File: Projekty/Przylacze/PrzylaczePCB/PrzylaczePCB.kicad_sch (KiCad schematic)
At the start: 9 parts, among them J1 Conn_01x06, J2 USB_B, U1 ATSAM4S2AA-AU

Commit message: Przyłącze - schemat elektryczny v1.0
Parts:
- removed C2: 2.2μ, symbol Device:C
- added C2: 4.7μ, Capacitor_THT:CP_Radial_Tantal_D5.0mm_P2.50mm, symbol Device:C_Polarized_US
- added C3: 2.2μ, Capacitor_THT:CP_Radial_Tantal_D5.0mm_P2.50mm, symbol Device:C_Polarized_US
- added D1, D2: LED, LED_SMD:LED_Kingbright_AAA3528ESGCT, symbol Device:LED
- added J1: Conn_02x04_Odd_Even, Connector_PinHeader_2.54mm:PinHeader_2x04_P2.54mm_Vertical, symbol Connector_Generic:Conn_02x04_Odd_Even
- added J2: Conn_02x20_Odd_Even, Connector_PinHeader_2.54mm:PinHeader_2x20_P2.54mm_Vertical, symbol Connector_Generic:Conn_02x20_Odd_Even
- added J5: Screw_Terminal_01x06, symbol Connector:Screw_Terminal_01x06
- added Q1, Q3, Q7, Q8: BC557, Package_TO_SOT_THT:TO-92_Inline, symbol Transistor_BJT:BC557
- added Q2, Q4: BC547, Package_TO_SOT_THT:TO-92_Inline, symbol Transistor_BJT:BC547
- added Q5, Q6: 2N3904, Package_TO_SOT_THT:TO-92_Inline, symbol Transistor_BJT:2N3904
- added R1, R10, R2, R3, R4, R9: 1k, Resistor_THT:R_Axial_DIN0207_L6.3mm_D2.5mm_P7.62mm_Horizontal, symbol Device:R
- added R5, R6: 360, Resistor_THT:R_Axial_DIN0207_L6.3mm_D2.5mm_P7.62mm_Horizontal, symbol Device:R
- added R7, R8: 470k, Resistor_THT:R_Axial_DIN0207_L6.3mm_D2.5mm_P7.62mm_Horizontal, symbol Device:R
- added SW1: SW_Push, Button_Switch_THT:SW_PUSH_6mm, symbol Switch:SW_Push
- added U1, U2: 74AHC1G04, PrzylaczeFootprintLibrary:Nexperia-SOT753-10_2018-0-0, symbol 74xGxx:74AHC1G04
- added U10: LDL1117S33R, Package_TO_SOT_SMD:SOT-223-3_TabPin2, symbol PrzylaczePCBLib:LDL1117S33R
- added U9: DI78M05UAB, Package_TO_SOT_SMD:SOT-89-3, symbol PrzylaczePCBLib:DI78M05UAB
- C1: value 4.7μ -> 100n; footprint (none) -> Capacitor_THT:C_Disc_D3.0mm_W1.6mm_P2.50mm
- J3: renamed from J1; footprint (none) -> Connector_PinHeader_2.54mm:PinHeader_1x06_P2.54mm_Horizontal
- J4: renamed from J2; footprint (none) -> Connector_USB:USB_B_OST_USB-B1HSxx_Horizontal
- R11: renamed from R1; footprint (none) -> Resistor_THT:R_Axial_DIN0207_L6.3mm_D2.5mm_P7.62mm_Horizontal
- R12: renamed from R2; footprint (none) -> Resistor_THT:R_Axial_DIN0207_L6.3mm_D2.5mm_P7.62mm_Horizontal
- R13: renamed from R3; footprint (none) -> Resistor_THT:R_Axial_DIN0207_L6.3mm_D2.5mm_P7.62mm_Horizontal
- R14: renamed from R4; footprint (none) -> Resistor_THT:R_Axial_DIN0207_L6.3mm_D2.5mm_P7.62mm_Horizontal
- U3: renamed from U1; footprint Microchip_Technology-ATSAM4S2AA-AU-* -> Package_QFP:LQFP-48_7x7mm_P0.5mm
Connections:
- net +3V3: now also C1.2, U3.33 (VDDIO), U3.47 (VDDIO), C2.1, J1.2 (Pin_2), J1.4 (Pin_4); no longer C1.1
- net CS0: now also J1.3 (Pin_3), J2.40 (Pin_40)
- net CS3: now also J2.38 (Pin_38)
- net MISO: now also J1.7 (Pin_7), J2.35 (Pin_35)
- net MOSI: now also J1.6 (Pin_6), J2.33 (Pin_33)
- net SPCK: now also J1.5 (Pin_5), J2.37 (Pin_37)
- net USBMON: now also U3.3 (PB0/AD4); no longer U3.31 (PA3)
- net at U3.18 (VDDCORE), U3.48 (VDDPLL), U3.8 (VDDOUT): now also U3.41 (VDDCORE), C3.1
- net RX/TX ENABLE : now reaches U3.28 (PA4/PGMNCMD)
- net at U3.29 (~{RST}): now also SW1.2
- net OPTO_R1: now reaches U3.32 (PA2/PGMEN2)
- net OPTO_R1: now also U3.31 (PA3), J2.16 (Pin_16), J2.18 (Pin_18), Q6.3 (C), R8.1
- net +5V: now reaches U3.34 (GND)
- net +5V: now also C1.1, J3.1 (Pin_1), J4.4 (GND), R14.2, U3.2 (GND), C2.2, C3.2, J1.1 (Pin_1), J5.6 (Pin_6), Q1.3 (E), Q2.3 (E), Q3.3 (E), Q4.3 (E), Q5.1 (E), Q6.1 (E), Q7.3 (E), Q8.3 (E), R7.2, R8.2, SW1.1, U1.3 (GND), U1.5 (VCC), U10.3 (Vin), U2.3 (GND), U2.5 (VCC), U9.1 (Vout), U9.2 (GND)
- net OPTO_SW2: now reaches U3.35 (PA1/PGMEN1)
- net OPTO_SW2: now also J2.14 (Pin_14), R1.2, R9.2, U1.2
- net OPTO_SW1: now reaches U3.36 (PA0/PGMEN0)
- net OPTO_SW1: now also J2.12 (Pin_12), R10.2, R2.2, U2.2
- net RADIO_IRQ: now reaches U3.4 (PB1/AD5)
- net RADIO_IRQ: now also J1.8 (Pin_8)
- net UART1_RX: now reaches U3.5 (PB2/AD6)
- net UART1_TX: now reaches U3.6 (PB3/AD7)
- net CS1 renamed UART0_RX
- net UART0_RX: now also J2.20 (Pin_20)
- net CS2 renamed UART0_TX
- net UART0_TX: now also J2.22 (Pin_22)
- removed net GND: C1.2, J3.1 (Pin_1), J4.4 (GND), R14.2, U3.2 (GND)
- new net: Q8.2 (B), R10.1
- new net: Q8.1 (C), R6.1
- new net: Q3.2 (B), R4.1
- new net: R4.2, U2.4
- new net: Q1.2 (B), R3.1
- new net: R3.2, U1.4
- new net: Q7.1 (C), R5.1
- new net: Q7.2 (B), R9.1
- new net: D2.1 (K), Q3.1 (C), Q4.1 (C)
- new net: Q4.2 (B), R2.1
- new net: D2.2 (A), Q6.2 (B), R6.2
- new net: D1.1 (K), Q1.1 (C), Q2.1 (C)
- new net: Q2.2 (B), R1.1
- new net: D1.2 (A), Q5.2 (B), R5.2
- new net +12V: J5.5 (Pin_5), U10.3 (Vin), U9.3 (Vin)
- new net +3.3V: U10.2 (Vout)
- new net A: J2.2 (Pin_2), J5.1 (Pin_1)
- new net B: J2.4 (Pin_4), J5.2 (Pin_2)
- new net CANH: J2.1 (Pin_1), J5.3 (Pin_3)
- new net CANL: J2.3 (Pin_3), J5.4 (Pin_4)
- new net EN: J2.13 (Pin_13)
- new net ERR: J2.15 (Pin_15)
- new net INT: J2.29 (Pin_29)
- new net OPTO_R2: Q5.3 (C), R7.1
- new net RESET: J2.39 (Pin_39)
- new net RX0BF: J2.23 (Pin_23)
- new net RX1BF: J2.25 (Pin_25)
- new net RXD: J2.7 (Pin_7)
- new net RX_MCU: J2.8 (Pin_8)
- new net RX/TX ENABLE: J2.10 (Pin_10)
- new net SOF: J2.27 (Pin_27)
- new net STB_FT: J2.9 (Pin_9)
- new net TX0RTS: J2.17 (Pin_17)
- new net TX1RTS: J2.19 (Pin_19)
- new net TX2RTS: J2.21 (Pin_21)
- new net TXD: J2.5 (Pin_5)
- new net TX_MCU: J2.6 (Pin_6)
- new net WAKE: J2.11 (Pin_11)
- no-connect marks 0 -> 15
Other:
- added sheet CAN (CAN.kicad_sch)
- added sheet EIA485 (EIA485.kicad_sch)
- note added: "C3 jak najbliżej złącza NRF24L01+ ma wymiary 30 x 16 mm"
- note added: "D1 i D2 dosyć blisko siebie na brzegu płytki"
- note added: "EIA485"
- note added: "JTAG"
- note added: "LISTWA UŻYTKOWNIKA"
- note added: "LISTWA WIĄZKI"
- note added: "Listwa użytkownika na przedniej krawędzi płytki Listwa wiązki, USB, JTAG na tylnej krawędzi płytki Złącze dla RADIO (moduł NRF24L01+) umieścić na tylnej krawędzi płytki tak, aby moduł wystawał poza nią (patrz obrazek po prawo)"
- note added: "Mikrokontroler"
- note added: "OPTO"
- note added: "OPTO EXT_MCU"
- note added: "RADIO"
- note added: "SPI RADIO & CAN"
- note added: "USB"
- note added: "Zasilanie"
- note added: "Złącza"
- moved on the sheet: J3, J4, R11, R12, R13, R14, U3

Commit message: Przyłącze - schemat elektryczny v1.1
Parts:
- J5: footprint (none) -> TerminalBlock:TerminalBlock_bornier-6_P5.08mm
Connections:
- net A: now also J2.1 (Pin_1)
- net B: now also J2.3 (Pin_3)
- net CANH: now also J2.5 (Pin_5), J2.6 (Pin_6); no longer J2.1 (Pin_1)
- net CANL: now also J2.7 (Pin_7), J2.8 (Pin_8); no longer J2.3 (Pin_3)
- net CS0: now also J2.36 (Pin_36); no longer J2.40 (Pin_40)
- net CS3: now also J2.34 (Pin_34); no longer J2.38 (Pin_38)
- net EN: now also J2.17 (Pin_17); no longer J2.13 (Pin_13)
- net ERR: now also J2.19 (Pin_19); no longer J2.15 (Pin_15)
- net INT: now also J2.33 (Pin_33); no longer J2.29 (Pin_29)
- net MISO: now also J2.30 (Pin_30); no longer J2.35 (Pin_35)
- net MOSI: now also J2.28 (Pin_28); no longer J2.33 (Pin_33)
- net OPTO_R1: now also J2.20 (Pin_20), J2.22 (Pin_22); no longer J2.16 (Pin_16), J2.18 (Pin_18)
- net OPTO_SW1: now also J2.16 (Pin_16); no longer J2.12 (Pin_12)
- net OPTO_SW2: now also J2.18 (Pin_18); no longer J2.14 (Pin_14)
- net RESET: now also J2.35 (Pin_35); no longer J2.39 (Pin_39)
- net RX0BF: now also J2.27 (Pin_27); no longer J2.23 (Pin_23)
- net RX1BF: now also J2.29 (Pin_29); no longer J2.25 (Pin_25)
- net RXD: now also J2.11 (Pin_11); no longer J2.7 (Pin_7)
- net RX_MCU: now also J2.12 (Pin_12); no longer J2.8 (Pin_8)
- net RX/TX ENABLE: now also J2.14 (Pin_14); no longer J2.10 (Pin_10)
- net SOF: now also J2.31 (Pin_31); no longer J2.27 (Pin_27)
- net SPCK: now also J2.32 (Pin_32); no longer J2.37 (Pin_37)
- net STB_FT: now also J2.13 (Pin_13); no longer J2.9 (Pin_9)
- net TX0RTS: now also J2.21 (Pin_21); no longer J2.17 (Pin_17)
- net TX1RTS: now also J2.23 (Pin_23); no longer J2.19 (Pin_19)
- net TX2RTS: now also J2.25 (Pin_25); no longer J2.21 (Pin_21)
- net TXD: now also J2.9 (Pin_9); no longer J2.5 (Pin_5)
- net TX_MCU: now also J2.10 (Pin_10); no longer J2.6 (Pin_6)
- net UART0_RX: now also J2.24 (Pin_24); no longer J2.20 (Pin_20)
- net UART0_TX: now also J2.26 (Pin_26); no longer J2.22 (Pin_22)
- net WAKE: now also J2.15 (Pin_15); no longer J2.11 (Pin_11)
- no-connect marks 15 -> 19
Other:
- note added: "C3 jak najbliżej złącza"
- note added: "Listwa użytkownika na przedniej krawędzi płytki Listwa wiązki, USB, JTAG na tylnej krawędzi płytki Złącze dla RADIO (moduł NRF24L01+) umieścić na tylnej krawędzi płytki tak, aby moduł wystawał poza nią (patrz obrazek po prawo) NRF24L01+ ma wymiary 30 x 16 mm"
- note removed: "C3 jak najbliżej złącza NRF24L01+ ma wymiary 30 x 16 mm"
- note removed: "Listwa użytkownika na przedniej krawędzi płytki Listwa wiązki, USB, JTAG na tylnej krawędzi płytki Złącze dla RADIO (moduł NRF24L01+) umieścić na tylnej krawędzi płytki tak, aby moduł wystawał poza nią (patrz obrazek po prawo)"
- moved on the sheet: R11, R12

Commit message: Przyłącze - schemat elektryczny v1.2
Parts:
- U3: footprint Package_QFP:LQFP-48_7x7mm_P0.5mm -> Microchip_Technology-ATSAM4S2AA-AU-*
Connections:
- net +3V3 is gone; now on net +3.3V: C1.2, C2.1, J1.2 (Pin_2), J1.4 (Pin_4), U3.13 (VDDIO), U3.33 (VDDIO), U3.47 (VDDIO), U3.7 (VDDIN)
- net +5V: no longer C1.1, C2.2, C3.2, J1.1 (Pin_1), J3.1 (Pin_1), J4.4 (GND), J5.6 (Pin_6), Q2.3 (E), Q4.3 (E), Q5.1 (E), Q6.1 (E), R14.2, SW1.1, U1.3 (GND), U10.3 (Vin), U2.3 (GND), U3.2 (GND), U3.34 (GND), U9.2 (GND)
- net at R12.2: now also J4.2 (D-); no longer J4.3 (D+)
- net at R11.2: now also J4.3 (D+); no longer J4.2 (D-)
- new net GND: C1.1, C2.2, C3.2, J1.1 (Pin_1), J3.1 (Pin_1), J5.6 (Pin_6), Q2.3 (E), Q4.3 (E), Q5.1 (E), Q6.1 (E), R14.2, SW1.1, U1.3 (GND), U10.3 (Vin), U2.3 (GND), U3.2 (GND), U3.34 (GND), U9.2 (GND)
- no-connect marks 19 -> 20
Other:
- moved on the sheet: D2, Q3, Q4, Q6, Q8, R10, R2, R4, R6, R8

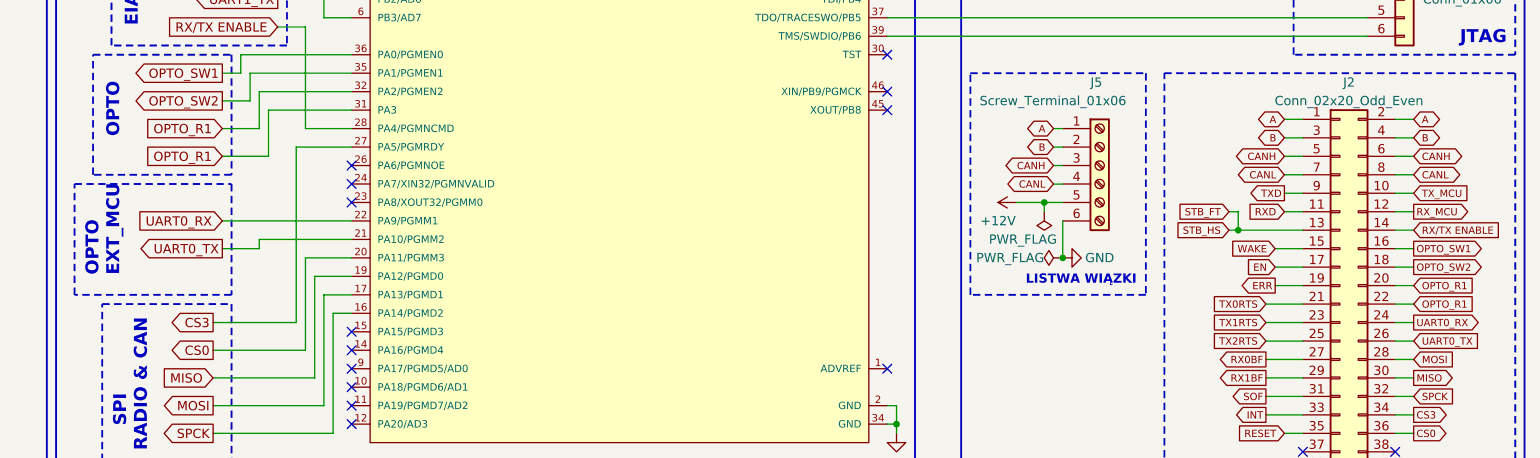
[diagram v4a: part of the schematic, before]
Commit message: Przyłącze - projekt PCB v0.1
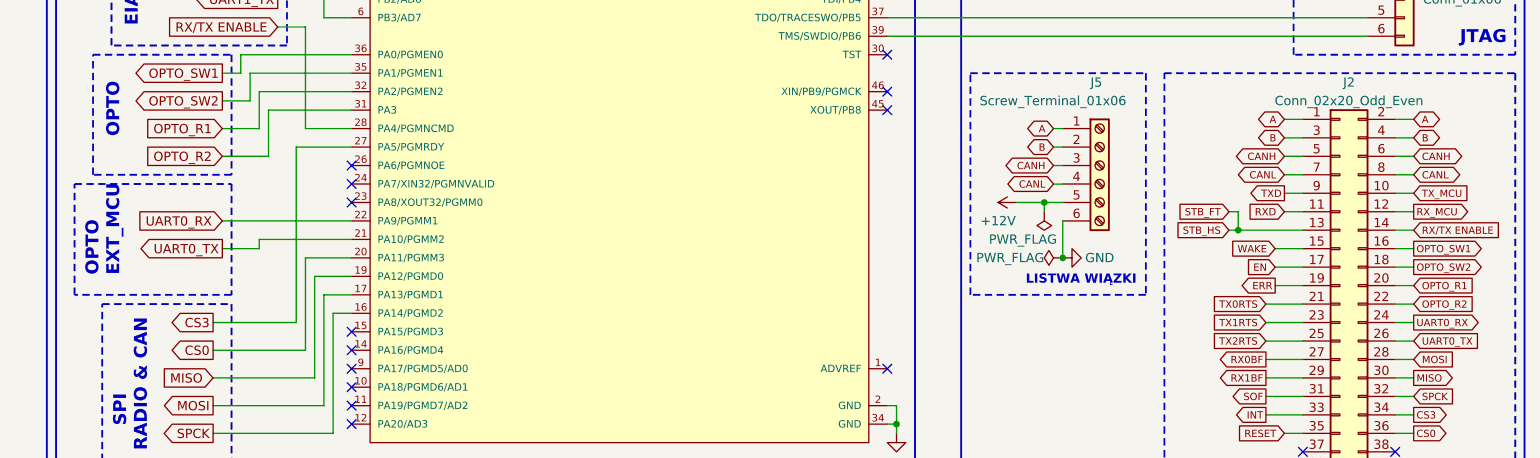
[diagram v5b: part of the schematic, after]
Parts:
- U3: footprint Microchip_Technology-ATSAM4S2AA-AU-* -> Package_QFP:LQFP-48_7x7mm_P0.5mm
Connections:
- net OPTO_R1: no longer J2.22 (Pin_22), U3.31 (PA3)
- net OPTO_R2: now also J2.22 (Pin_22), U3.31 (PA3)
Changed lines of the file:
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@@
     )
   )
-  (global_label "OPTO_R1" (shape input) (at 264.16 107.95 0) (fields_autoplaced)
+  (global_label "OPTO_R2" (shape input) (at 264.16 107.95 0) (fields_autoplaced)
     (effects (font (size 0.9906 0.9906)) (justify left))
     (property "Intersheetrefs" "${INTERSHEET_REFS}" (at 272.936 107.95 0)
@@
     )
   )
-  (global_label "OPTO_R1" (shape input) (at 100.33 87.63 180) (fields_autoplaced)
+  (global_label "OPTO_R2" (shape input) (at 100.33 87.63 180) (fields_autoplaced)
     (effects (font (size 1.27 1.27)) (justify right))
     (property "Intersheetrefs" "${INTERSHEET_REFS}" (at 89.0785 87.63 0)
@@
       (effects (font (size 1.27 1.27)))
     )
-    (property "Footprint" "Microchip_Technology-ATSAM4S2AA-AU-*" (at 115.57 27.94 0)
-      (effects (font (size 1.27 1.27)) (justify left) hide)
-    )
+    (property "Footprint" "Package_QFP:LQFP-48_7x7mm_P0.5mm" (at 115.57 27.94 0)
+      (effects (font (size 1.27 1.27)) (justify left) hide)
+    )

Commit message: Przyłącze - projekt PCB v0.2
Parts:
- J2: footprint Connector_PinHeader_2.54mm:PinHeader_2x20_P2.54mm_Vertical -> Connector_PinHeader_2.54mm:PinHeader_2x20_P2.54mm_Horizontal
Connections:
- net CANH: now also J5.4 (Pin_4); no longer J5.3 (Pin_3)
- net CANL: now also J5.3 (Pin_3); no longer J5.4 (Pin_4)
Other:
- note added: "C1 jak najbliżej złącza"
- note removed: "C3 jak najbliżej złącza"

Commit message: Przyłącze - projekt PCB v0.3
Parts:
- J3: footprint Connector_PinHeader_2.54mm:PinHeader_1x06_P2.54mm_Horizontal -> Connector_PinHeader_2.54mm:PinHeader_1x06_P2.54mm_Vertical
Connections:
- net +3.3V: no longer U3.33 (VDDIO), U3.47 (VDDIO)
- net A: now also J5.4 (Pin_4); no longer J5.1 (Pin_1)
- net B: now also J5.3 (Pin_3); no longer J5.2 (Pin_2)
- net CANH: now also J5.1 (Pin_1); no longer J5.4 (Pin_4)
- net CANL: now also J5.2 (Pin_2); no longer J5.3 (Pin_3)
- net GND: now also U10.1 (GND); no longer U10.3 (Vin)
- net at C3.1, U3.18 (VDDCORE), U3.48 (VDDPLL)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: no longer U3.41 (VDDCORE)
- no-connect marks 20 -> 23
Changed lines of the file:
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@@
 (kicad_sch (version 20230121) (generator eeschema)
   (paper "A4")
-  (junction (at 116.84 45.72) (diameter 0) (color 0 0 0 0)
-  )
-  (junction (at 116.84 38.1) (diameter 0) (color 0 0 0 0)
-  )
   (junction (at 33.02 147.32) (diameter 0) (color 0 0 0 0)
   )
@@
   (junction (at 267.97 25.4) (diameter 0) (color 0 0 0 0)
   )
-  (junction (at 116.84 48.26) (diameter 0) (color 0 0 0 0)
-  )
   (junction (at 33.02 110.49) (diameter 0) (color 0 0 0 0)
   )
@@
   )
   (no_connect (at 227.33 53.34))
+  (no_connect (at 118.11 50.8))
   (no_connect (at 118.11 91.44))
   (no_connect (at 118.11 93.98))
@@
   (no_connect (at 261.62 130.81))
   (no_connect (at 191.77 81.28))
+  (no_connect (at 118.11 48.26))
   (no_connect (at 191.77 53.34))
   (no_connect (at 118.11 121.92))
+  (no_connect (at 118.11 40.64))
   (no_connect (at 191.77 116.84))
   (no_connect (at 191.77 78.74))
@@
     (stroke (width 0) (type default))
   )
-  (wire (pts (xy 116.84 50.8) (xy 116.84 48.26))
-    (stroke (width 0) (type default))
-  )
   (wire (pts (xy 53.34 73.66) (xy 57.15 73.66))
     (stroke (width 0) (type default))
@@
     (stroke (width 0) (type default))
   )
-  (wire (pts (xy 116.84 38.1) (xy 118.11 38.1))
+  (wire (pts (xy 111.76 38.1) (xy 118.11 38.1))
     (stroke (width 0) (type default))
   )
@@
     (stroke (width 0) (type default))
   )
-  (wire (pts (xy 118.11 40.64) (xy 116.84 40.64))
-    (stroke (width 0) (type default))
-  )
-  (wire (pts (xy 116.84 45.72) (xy 118.11 45.72))
+  (wire (pts (xy 107.95 45.72) (xy 118.11 45.72))
     (stroke (width 0) (type default))
   )
@@
     (stroke (width 0) (type default))
   )
-  (wire (pts (xy 111.76 38.1) (xy 116.84 38.1))
-    (stroke (width 0) (type default))
-  )
   (wire (pts (xy 261.62 97.79) (xy 264.16 97.79))
     (stroke (width 0) (type default))
@@
     (stroke (width 0) (type default))
   )
-  (wire (pts (xy 107.95 45.72) (xy 116.84 45.72))
-    (stroke (width 0) (type default))
-  )
   (wire (pts (xy 193.04 125.73) (xy 193.04 124.46))
     (stroke (width 0) (type default))
@@
     (stroke (width 0) (type default))
   )
-  (wire (pts (xy 118.11 48.26) (xy 116.84 48.26))
-    (stroke (width 0) (type default))
-  )
   (wire (pts (xy 55.88 16.51) (xy 55.88 30.48))
     (stroke (width 0) (type default))
   )
-  (wire (pts (xy 116.84 48.26) (xy 116.84 45.72))
-    (stroke (width 0) (type default))
-  )
   (wire (pts (xy 274.32 40.64) (xy 274.32 39.37))
     (stroke (width 0) (type default))
@@
     (stroke (width 0) (type default))
   )
-  (wire (pts (xy 116.84 40.64) (xy 116.84 38.1))
-    (stroke (width 0) (type default))
-  )
   (wire (pts (xy 33.02 60.96) (xy 35.56 60.96))
     (stroke (width 0) (type default))
@@
     (stroke (width 0) (type default))
   )
-  (wire (pts (xy 118.11 50.8) (xy 116.84 50.8))
-    (stroke (width 0) (type default))
-  )
   (wire (pts (xy 105.41 43.18) (xy 107.95 43.18))
     (stroke (width 0) (type default))
@@
     )
   )
-  (global_label "CANH" (shape bidirectional) (at 214.63 91.44 180) (fields_autoplaced)
+  (global_label "CANH" (shape bidirectional) (at 214.63 83.82 180) (fields_autoplaced)
     (effects (font (size 0.9906 0.9906)) (justify right))
-    (property "Intersheetrefs" "${INTERSHEET_REFS}" (at 207.5815 91.44 0)
+    (property "Intersheetrefs" "${INTERSHEET_REFS}" (at 207.5815 83.82 0)
       (effects (font (size 1.27 1.27)) (justify right) hide)
     )
@@
     )
   )
-  (global_label "B" (shape bidirectional) (at 214.63 86.36 180) (fields_autoplaced)
+  (global_label "B" (shape bidirectional) (at 214.63 88.9 180) (fields_autoplaced)
     (effects (font (size 0.9906 0.9906)) (justify right))
-    (property "Intersheetrefs" "${INTERSHEET_REFS}" (at 210.5062 86.36 0)
+    (property "Intersheetrefs" "${INTERSHEET_REFS}" (at 210.5062 88.9 0)
       (effects (font (size 1.27 1.27)) (justify right) hide)
     )
@@
     )
   )
-  (global_label "CANL" (shape bidirectional) (at 214.63 88.9 180) (fields_autoplaced)
+  (global_label "CANL" (shape bidirectional) (at 214.63 86.36 180) (fields_autoplaced)
     (effects (font (size 0.9906 0.9906)) (justify right))
-    (property "Intersheetrefs" "${INTERSHEET_REFS}" (at 207.8174 88.9 0)
+    (property "Intersheetrefs" "${INTERSHEET_REFS}" (at 207.8174 86.36 0)
       (effects (font (size 1.27 1.27)) (justify right) hide)
     )
@@
     )
   )
-  (global_label "A" (shape bidirectional) (at 214.63 83.82 180) (fields_autoplaced)
+  (global_label "A" (shape bidirectional) (at 214.63 91.44 180) (fields_autoplaced)
     (effects (font (size 0.9906 0.9906)) (justify right))
-    (property "Intersheetrefs" "${INTERSHEET_REFS}" (at 210.6477 83.82 0)
+    (property "Intersheetrefs" "${INTERSHEET_REFS}" (at 210.6477 91.44 0)
       (effects (font (size 1.27 1.27)) (justify right) hide)
     )
@@
       (effects (font (size 1.27 1.27)) hide)
     )
+    (pin "1")
     (pin "2")
     (pin "3")
-    (pin "3")
     (instances
       (project "PrzylaczePCB"
@@
       (effects (font (size 1.27 1.27)) (justify left))
     )
-    (property "Footprint" "Connector_PinHeader_2.54mm:PinHeader_1x06_P2.54mm_Horizontal" (at 262.89 63.5 0)
+    (property "Footprint" "Connector_PinHeader_2.54mm:PinHeader_1x06_P2.54mm_Vertical" (at 262.89 63.5 0)
       (effects (font (size 1.27 1.27)) hide)
     )
